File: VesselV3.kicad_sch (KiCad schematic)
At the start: 375 parts, among them J1 JTAG/SWD 10pins Headers, Y1 25MHz

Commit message: Fixed Bottom Left Mounting hole and Adjusted PMMA
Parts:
- H2: footprint MountingHole:MountingHole_6.5mm -> MountingHole:MountingHole_7mm
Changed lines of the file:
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@@
       (effects (font (size 1.27 1.27)) (justify left))
     )
-    (property "Footprint" "MountingHole:MountingHole_6.5mm" (at 426.72 204.47 0)
+    (property "Footprint" "MountingHole:MountingHole_7mm" (at 426.72 204.47 0)
       (effects (font (size 1.27 1.27)) hide)
     )

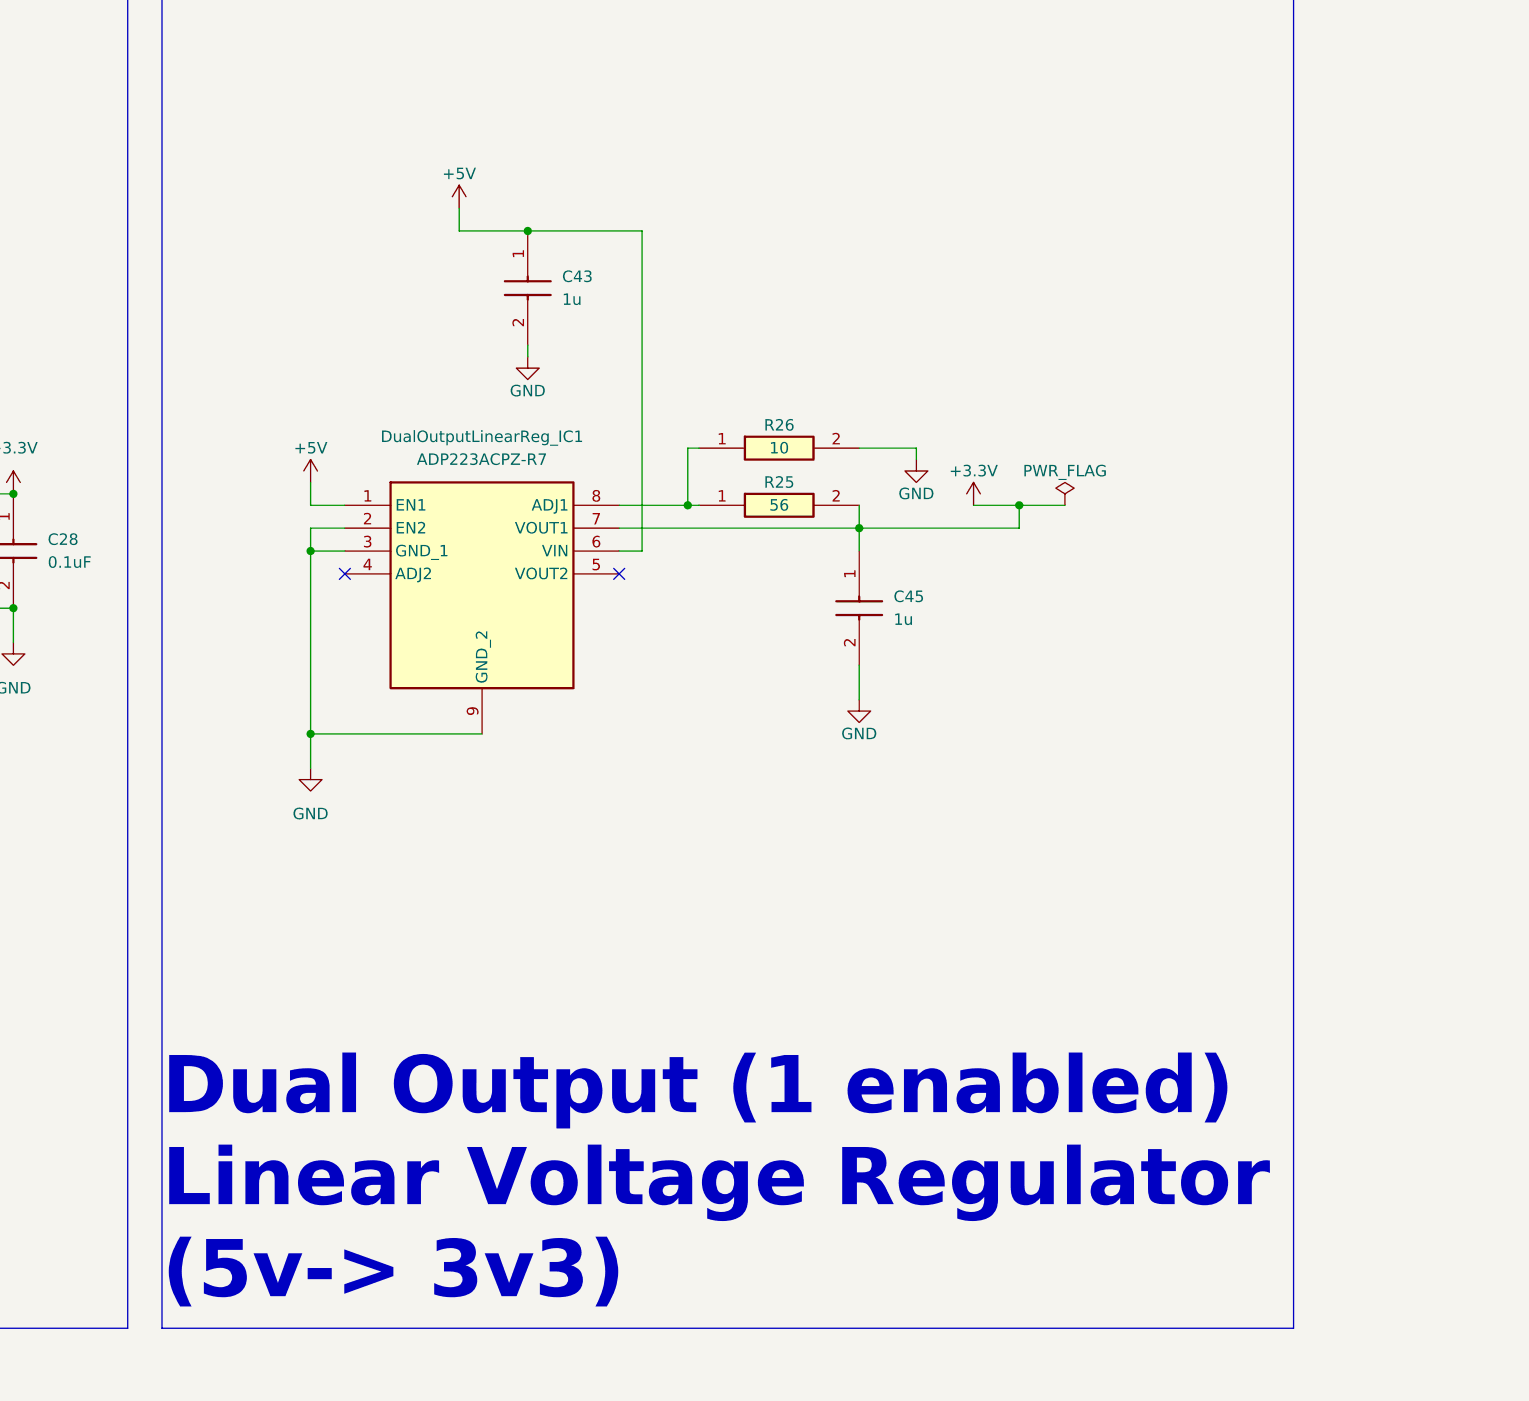
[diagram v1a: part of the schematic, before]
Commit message: Swapped QFN 3v3 Linear Reg for SOT25 3v3 LDO Reg
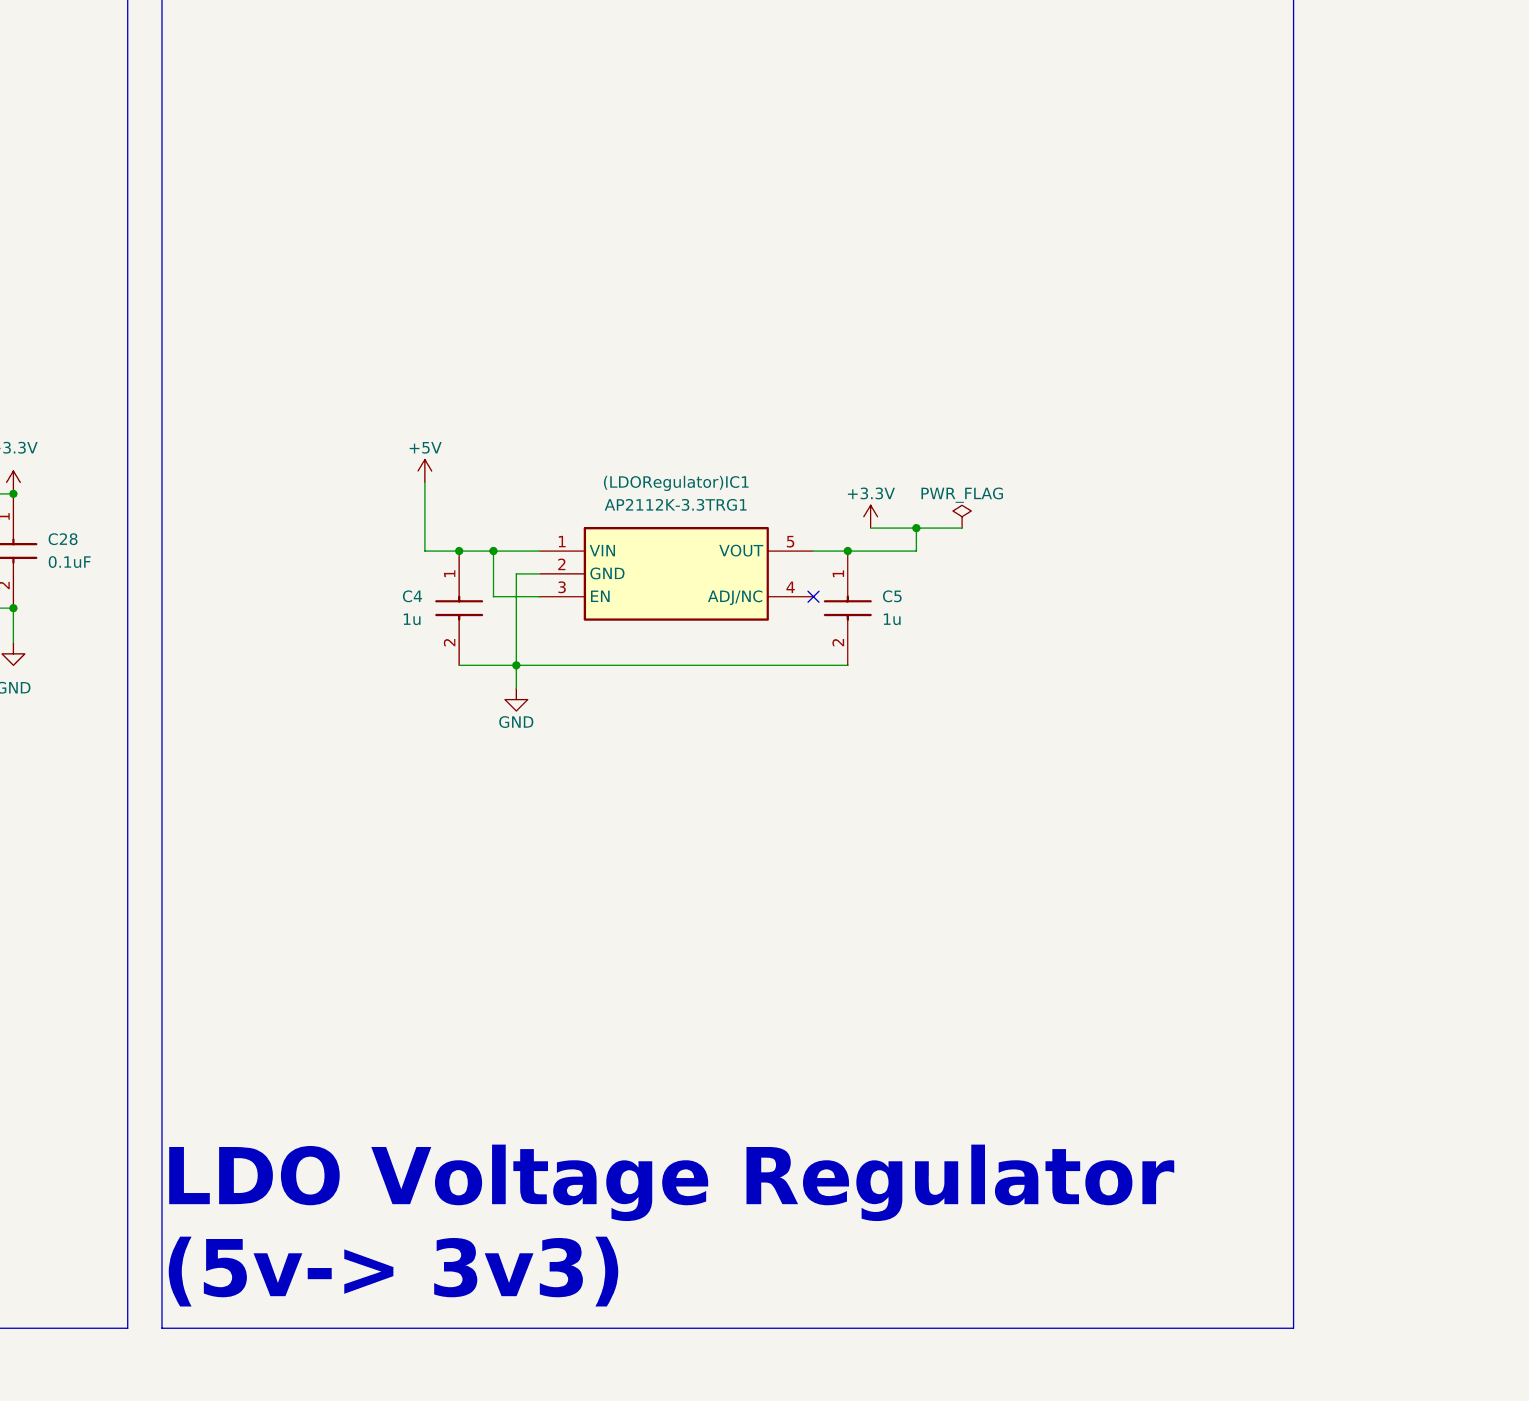
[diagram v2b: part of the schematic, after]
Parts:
- removed C43, C45: 1u, SamacSys_Parts:CAPC2012X140N, symbol SamacSys_Parts:0805ZC105JAT2A
- removed DualOutputLinearReg_IC1: ADP223ACPZ-R7, SamacSys_Parts:SON50P200X200X65-9N-D, symbol SamacSys_Parts:ADP223ACPZ-R7
- removed R25: 56, SamacSys_Parts:RESC2012X50N, symbol SamacSys_Parts:CRCW080556R0FKEA
- removed R26: 10, SamacSys_Parts:RESC2012X50N, symbol SamacSys_Parts:CRCW080510R0FKEA
- added (LDORegulator)IC1: AP2112K-3.3TRG1, SOT95P282X130-5N, symbol SamacSys_Parts:AP2112K-3.3TRG1
- added C4, C5: 1u, SamacSys_Parts:CAPC2012X140N, symbol SamacSys_Parts:0805ZC105JAT2A
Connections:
- net +3.3V: now also (LDORegulator)IC1.5 (VOUT), C5.1
- net +5V: now also (LDORegulator)IC1.1 (VIN), (LDORegulator)IC1.3 (EN), C4.1
- net GND: now also (LDORegulator)IC1.2 (GND), C4.2, C5.2
- no-connect marks 31 -> 30
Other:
- note added: "LDO Voltage Regulator (5v-> 3v3)"
- note removed: "Dual Output (1 enabled) Linear Voltage Regulator (5v-> 3v3)"

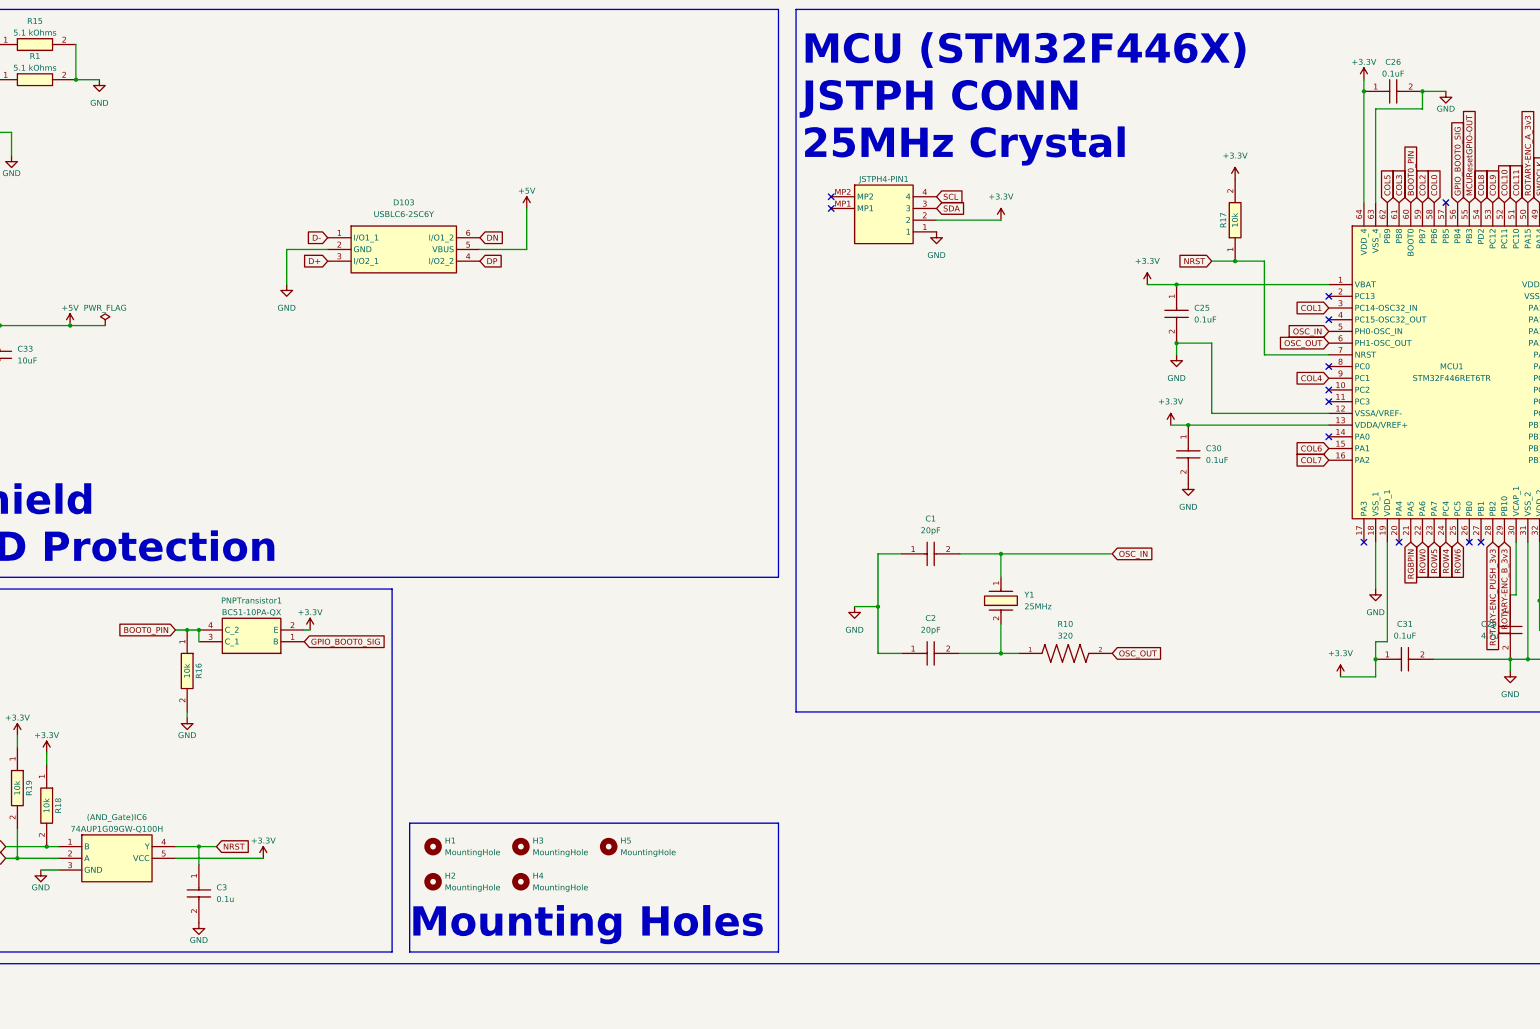
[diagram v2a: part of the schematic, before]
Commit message: PCB : +4 Solder jumpers, -RPd (NRST), Routing fix
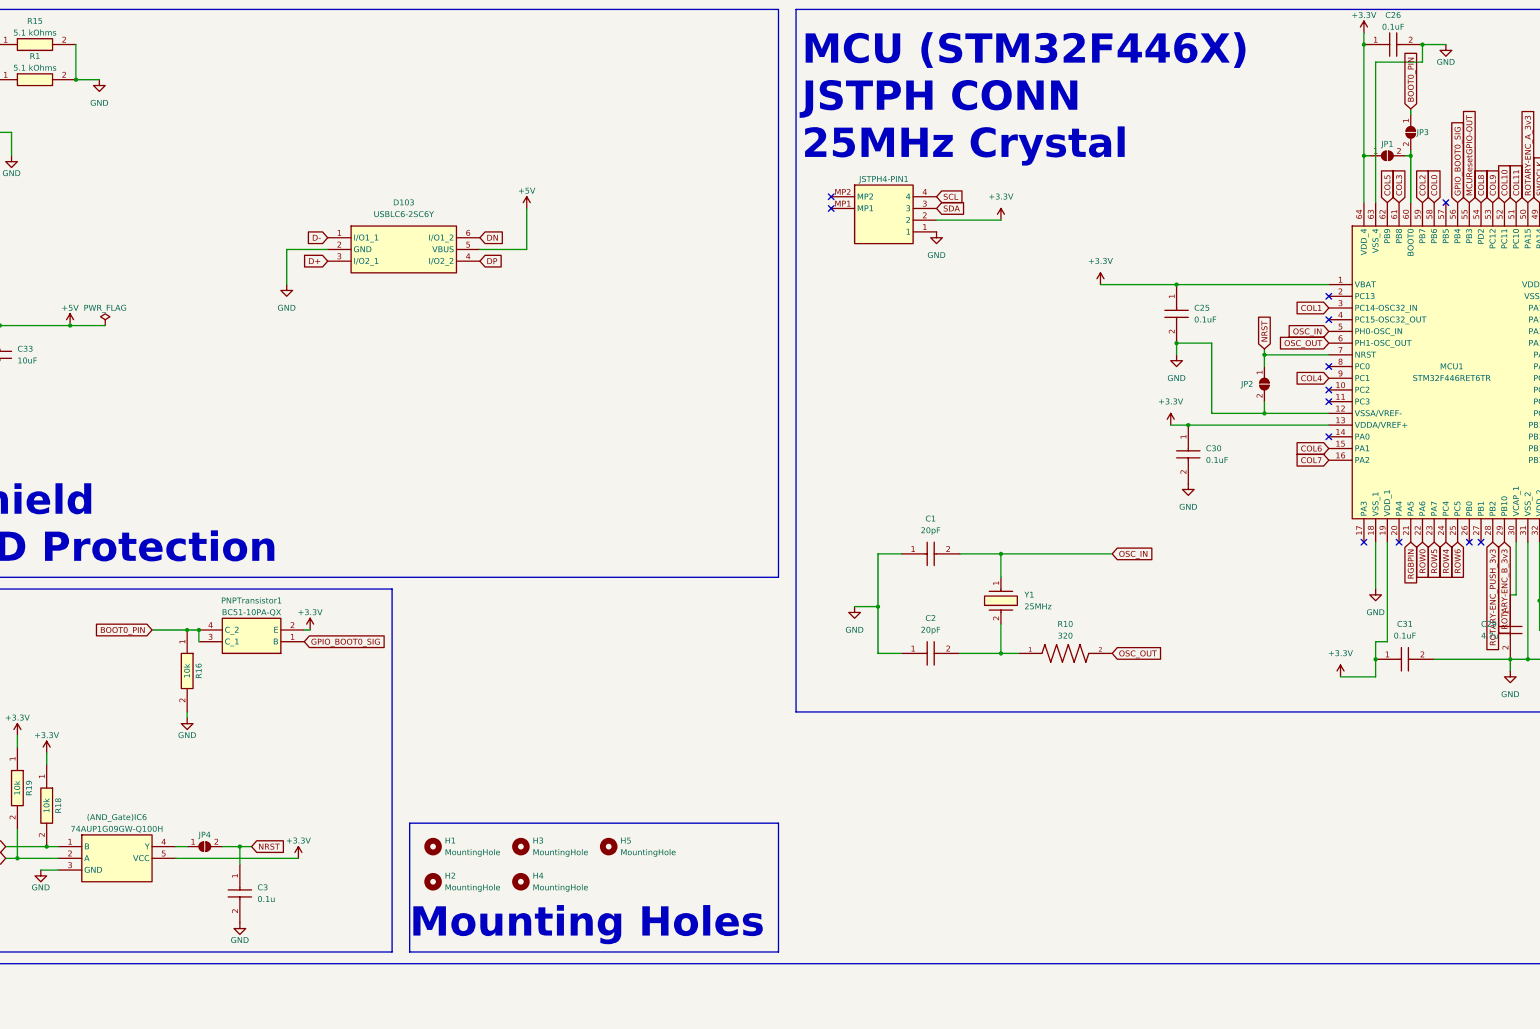
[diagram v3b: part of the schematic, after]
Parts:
- removed R17: 10k, SamacSys_Parts:RESC2012X50N, symbol SamacSys_Parts:CRCW080510K0JNEC
- added JP1: Boot0 to 3v3_1, Jumper:SolderJumper-2_P1.3mm_Open_TrianglePad1.0x1.5mm, symbol Jumper:SolderJumper_2_Open
- added JP2: NRST to GND_2, Jumper:SolderJumper-2_P1.3mm_Open_TrianglePad1.0x1.5mm, symbol Jumper:SolderJumper_2_Open
- added JP3: Boot0 to PNP_3, Jumper:SolderJumper-2_P1.3mm_Open_TrianglePad1.0x1.5mm, symbol Jumper:SolderJumper_2_Open
- added JP4: NRST to AND_4, Jumper:SolderJumper-2_P1.3mm_Open_TrianglePad1.0x1.5mm, symbol Jumper:SolderJumper_2_Open
- (LDORegulator)IC1: footprint SOT95P282X130-5N -> SamacSys_Parts:SOT95P282X130-5N
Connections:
- net +3.3V: now also JP1.1 (A)
- net BOOT0_PIN: now also JP3.1 (A); no longer MCU1.60 (BOOT0)
- net GND: now also JP2.2 (B)
- net NRST: now also JP2.1 (A), JP4.2 (B); no longer (AND_Gate)IC6.4 (Y)
- new net: JP1.2 (B), JP3.2 (B), MCU1.60 (BOOT0)
- new net: (AND_Gate)IC6.4 (Y), JP4.1 (A)
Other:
- moved on the sheet: C26, C3
